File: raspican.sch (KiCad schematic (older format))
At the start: 26 parts, among them J1 CANBUS, J2 TTL_SERIAL, J3 TERMINATE, P1 CONN_13X2, SW1 BUTTON_FRAME, SW2 BUTTON_FRAME, U1 MCP2551-I/P, U4 MCP2515, Y1 16MHz

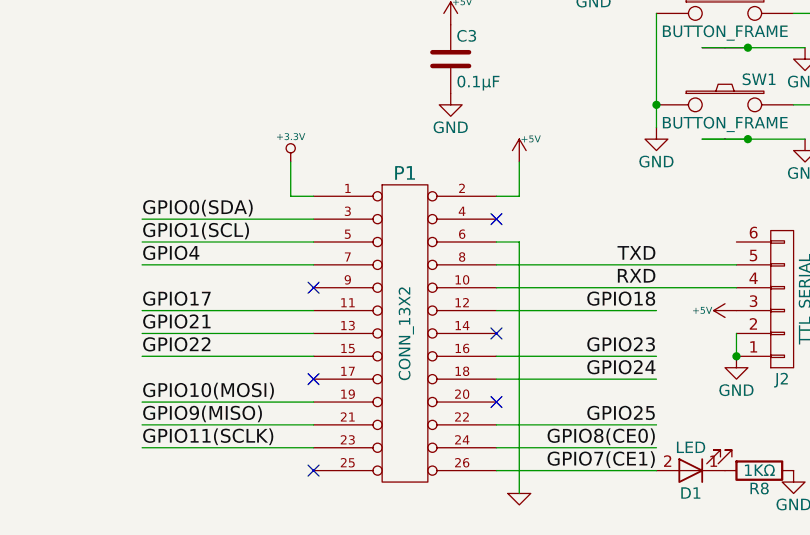
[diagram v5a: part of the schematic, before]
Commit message: template was wrong about P1 connections
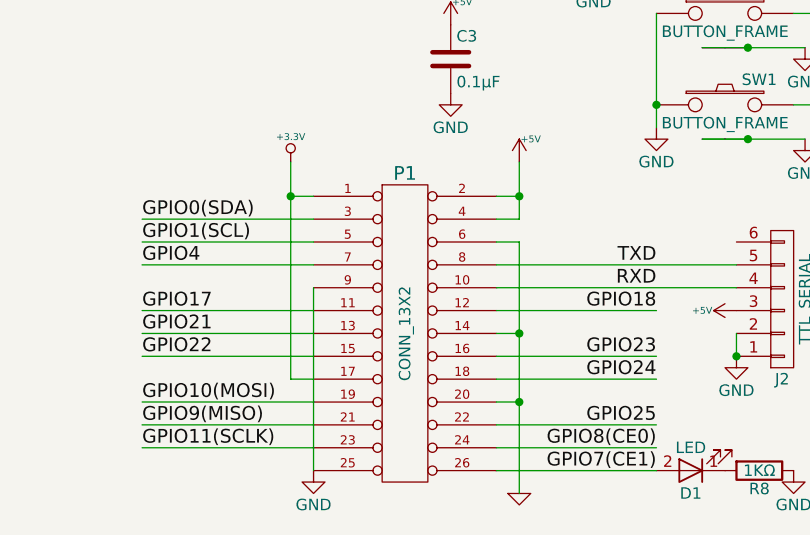
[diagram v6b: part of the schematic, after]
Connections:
- net +3.3V: now also P1.17 (P17)
- net +5V: now also P1.4 (P4)
- net GND: now also P1.14 (P14), P1.20 (P20), P1.25 (P24), P1.9 (P9)
- no-connect marks 6 -> 0
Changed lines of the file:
@@
 $EndComp
 Wire Wire Line
-	1900 5900 1900 6050
+	1900 5900 1900 6850
 Wire Wire Line
 	1900 6050 2000 6050
@@
 $EndComp
 Wire Wire Line
-	2900 5900 2900 6050
+	2900 5900 2900 6150
 Wire Wire Line
 	2900 6050 2800 6050
-NoConn ~ 2800 6150
 Wire Wire Line
 	2000 6150 1250 6150
@@
 Text Label 1250 6350 0    60   ~ 0
 GPIO4
-NoConn ~ 2000 6450
 Wire Wire Line
 	2000 6550 1250 6550
@@
 Text Label 1250 6750 0    60   ~ 0
 GPIO22
-NoConn ~ 2000 6850
 Wire Wire Line
 	2000 6950 1250 6950
@@
 Text Label 1250 7150 0    60   ~ 0
 GPIO11(SCLK)
-NoConn ~ 2000 7250
 $Comp
 L GND-RESCUE-raspican #PWR03
@@
 Text Label 3500 6550 2    60   ~ 0
 GPIO18
-NoConn ~ 2800 6650
 Wire Wire Line
 	2800 6750 3500 6750
@@
 Text Label 3500 6850 2    60   ~ 0
 GPIO24
-NoConn ~ 2800 6950
 Wire Wire Line
 	2800 7050 3500 7050
@@
 Wire Wire Line
 	3625 3550 3625 3750
+Wire Wire Line
+	2900 6150 2800 6150
+Connection ~ 2900 6050
+$Comp
+L GND #PWR?
+U 1 1 58C78B04
+P 2000 7250
+F 0 "#PWR?" H 2000 7000 50  0001 C CNN
+F 1 "GND" H 2000 7100 50  0000 C CNN
+F 2 "" H 2000 7250 50  0001 C CNN
+F 3 "" H 2000 7250 50  0001 C CNN
+	1    2000 7250
+	1    0    0    -1
+$EndComp
+Connection ~ 2900 6650
+Connection ~ 2900 6950
+Wire Wire Line
+	2800 6650 2900 6650
+Wire Wire Line
+	2900 6950 2800 6950
+Connection ~ 1900 6050
+Wire Wire Line
+	1900 6850 2000 6850
+Wire Wire Line
+	2000 6450 2000 7250
 $EndSCHEMATC
